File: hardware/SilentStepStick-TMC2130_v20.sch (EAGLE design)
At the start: 25 parts, among them IC1 TMC2130-LA, J1 MA08-1, J2 MA08-1, J3 MA02-1, X1 PASSER-07, X2 PASSER-07

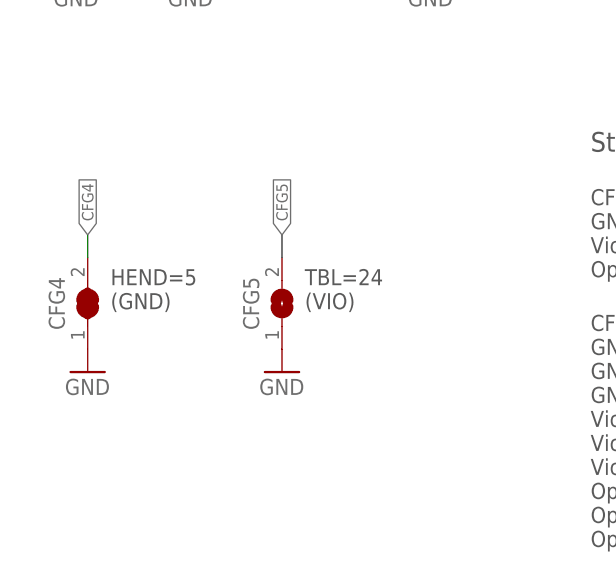
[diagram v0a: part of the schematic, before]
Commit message: updated schematics
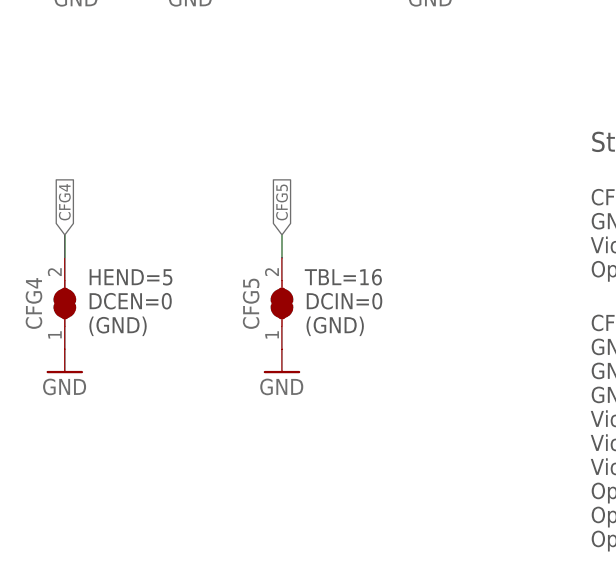
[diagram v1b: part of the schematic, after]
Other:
- note added: "HEND=5 DCEN=0 (GND)"
- note added: "TBL=16 DCIN=0 (GND)"
- note removed: "HEND=5 (GND)"
- note removed: "TBL=24 (VIO)"
- moved on the sheet: CFG4
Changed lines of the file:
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@@
 <grid distance="0.1" unitdist="inch" unit="inch" style="lines" multiple="1" display="no" altdistance="0.01" altunitdist="inch" altunit="inch"/>
 <layers>
-<layer number="1" name="Top" color="4" fill="1" visible="yes" active="no"/>
-<layer number="2" name="Route2" color="11" fill="1" visible="yes" active="no"/>
-<layer number="3" name="Route3" color="4" fill="3" visible="yes" active="no"/>
-<layer number="4" name="Route4" color="1" fill="4" visible="yes" active="no"/>
-<layer number="5" name="Route5" color="4" fill="4" visible="yes" active="no"/>
-<layer number="6" name="Route6" color="1" fill="8" visible="yes" active="no"/>
-<layer number="7" name="Route7" color="4" fill="8" visible="yes" active="no"/>
-<layer number="8" name="Route8" color="1" fill="2" visible="yes" active="no"/>
-<layer number="9" name="Route9" color="4" fill="2" visible="yes" active="no"/>
-<layer number="10" name="Route10" color="1" fill="7" visible="yes" active="no"/>
-<layer number="11" name="Route11" color="4" fill="7" visible="yes" active="no"/>
-<layer number="12" name="Route12" color="1" fill="5" visible="yes" active="no"/>
-<layer number="13" name="Route13" color="4" fill="5" visible="yes" active="no"/>
-<layer number="14" name="Route14" color="1" fill="6" visible="yes" active="no"/>
-<layer number="15" name="Route15" color="13" fill="1" visible="yes" active="no"/>
-<layer number="16" name="Bottom" color="1" fill="1" visible="yes" active="no"/>
-<layer number="17" name="Pads" color="2" fill="1" visible="yes" active="no"/>
-<layer number="18" name="Vias" color="2" fill="1" visible="yes" active="no"/>
-<layer number="19" name="Unrouted" color="14" fill="1" visible="yes" active="no"/>
-<layer number="20" name="Dimension" color="15" fill="1" visible="yes" active="no"/>
-<layer number="21" name="tPlace" color="7" fill="1" visible="yes" active="no"/>
-<layer number="22" name="bPlace" color="7" fill="1" visible="yes" active="no"/>
-<layer number="23" name="tOrigins" color="15" fill="1" visible="yes" active="no"/>
-<layer number="24" name="bOrigins" color="15" fill="1" visible="yes" active="no"/>
-<layer number="25" name="tNames" color="7" fill="1" visible="yes" active="no"/>
-<layer number="26" name="bNames" color="7" fill="1" visible="yes" active="no"/>
-<layer number="27" name="tValues" color="7" fill="1" visible="yes" active="no"/>
-<layer number="28" name="bValues" color="7" fill="1" visible="yes" active="no"/>
+<layer number="1" name="Top" color="4" fill="1" visible="no" active="no"/>
+<layer number="2" name="Route2" color="11" fill="1" visible="no" active="no"/>
+<layer number="3" name="Route3" color="4" fill="3" visible="no" active="no"/>
+<layer number="4" name="Route4" color="1" fill="4" visible="no" active="no"/>
+<layer number="5" name="Route5" color="4" fill="4" visible="no" active="no"/>
+<layer number="6" name="Route6" color="1" fill="8" visible="no" active="no"/>
+<layer number="7" name="Route7" color="4" fill="8" visible="no" active="no"/>
+<layer number="8" name="Route8" color="1" fill="2" visible="no" active="no"/>
+<layer number="9" name="Route9" color="4" fill="2" visible="no" active="no"/>
+<layer number="10" name="Route10" color="1" fill="7" visible="no" active="no"/>
+<layer number="11" name="Route11" color="4" fill="7" visible="no" active="no"/>
+<layer number="12" name="Route12" color="1" fill="5" visible="no" active="no"/>
+<layer number="13" name="Route13" color="4" fill="5" visible="no" active="no"/>
+<layer number="14" name="Route14" color="1" fill="6" visible="no" active="no"/>
+<layer number="15" name="Route15" color="13" fill="1" visible="no" active="no"/>
+<layer number="16" name="Bottom" color="1" fill="1" visible="no" active="no"/>
+<layer number="17" name="Pads" color="2" fill="1" visible="no" active="no"/>
+<layer number="18" name="Vias" color="2" fill="1" visible="no" active="no"/>
+<layer number="19" name="Unrouted" color="14" fill="1" visible="no" active="no"/>
+<layer number="20" name="Dimension" color="15" fill="1" visible="no" active="no"/>
+<layer number="21" name="tPlace" color="7" fill="1" visible="no" active="no"/>
+<layer number="22" name="bPlace" color="7" fill="1" visible="no" active="no"/>
+<layer number="23" name="tOrigins" color="15" fill="1" visible="no" active="no"/>
+<layer number="24" name="bOrigins" color="15" fill="1" visible="no" active="no"/>
+<layer number="25" name="tNames" color="7" fill="1" visible="no" active="no"/>
+<layer number="26" name="bNames" color="7" fill="1" visible="no" active="no"/>
+<layer number="27" name="tValues" color="7" fill="1" visible="no" active="no"/>
+<layer number="28" name="bValues" color="7" fill="1" visible="no" active="no"/>
 <layer number="29" name="tStop" color="7" fill="3" visible="no" active="no"/>
 <layer number="30" name="bStop" color="7" fill="6" visible="no" active="no"/>
@@
 <layer number="35" name="tGlue" color="7" fill="4" visible="no" active="no"/>
 <layer number="36" name="bGlue" color="7" fill="5" visible="no" active="no"/>
-<layer number="37" name="tTest" color="7" fill="1" visible="yes" active="no"/>
-<layer number="38" name="bTest" color="7" fill="1" visible="yes" active="no"/>
+<layer number="37" name="tTest" color="7" fill="1" visible="no" active="no"/>
+<layer number="38" name="bTest" color="7" fill="1" visible="no" active="no"/>
 <layer number="39" name="tKeepout" color="4" fill="11" visible="no" active="no"/>
 <layer number="40" name="bKeepout" color="1" fill="11" visible="no" active="no"/>
@@
 <layer number="44" name="Drills" color="7" fill="1" visible="no" active="no"/>
 <layer number="45" name="Holes" color="7" fill="1" visible="no" active="no"/>
-<layer number="46" name="Milling" color="3" fill="1" visible="yes" active="no"/>
-<layer number="47" name="Measures" color="7" fill="1" visible="yes" active="no"/>
-<layer number="48" name="Document" color="7" fill="1" visible="yes" active="no"/>
-<layer number="49" name="Reference" color="7" fill="1" visible="yes" active="no"/>
-<layer number="50" name="dxf" color="7" fill="1" visible="yes" active="no"/>
-<layer number="51" name="tDocu" color="7" fill="1" visible="yes" active="no"/>
-<layer number="52" name="bDocu" color="7" fill="1" visible="yes" active="no"/>
+<layer number="46" name="Milling" color="3" fill="1" visible="no" active="no"/>
+<layer number="47" name="Measures" color="7" fill="1" visible="no" active="no"/>
+<layer number="48" name="Document" color="7" fill="1" visible="no" active="no"/>
+<layer number="49" name="Reference" color="7" fill="1" visible="no" active="no"/>
+<layer number="50" name="dxf" color="7" fill="1" visible="no" active="no"/>
+<layer number="51" name="tDocu" color="7" fill="1" visible="no" active="no"/>
+<layer number="52" name="bDocu" color="7" fill="1" visible="no" active="no"/>
 <layer number="90" name="Modules" color="5" fill="1" visible="yes" active="yes"/>
 <layer number="91" name="Nets" color="2" fill="1" visible="yes" active="yes"/>
@@
 <layer number="98" name="Guide" color="6" fill="1" visible="yes" active="yes"/>
 <layer number="99" name="SpiceOrder" color="5" fill="1" visible="yes" active="yes"/>
-<layer number="250" name="Descript" color="3" fill="1" visible="yes" active="yes"/>
 </layers>
 <schematic xreflabel="%F%N/%S.%C%R" xrefpart="/%S.%C%R">
@@
 <sheet>
 <plain>
-<wire x1="34.29" y1="36.83" x2="34.29" y2="39.37" width="1.016" layer="94"/>
+<wire x1="31.75" y1="36.83" x2="31.75" y2="39.37" width="1.016" layer="94"/>
 <text x="162.56" y="22.86" size="1.27" layer="95" align="top-left">Released under the Creative Commons Attribution Share-Alike
 License. http://creativecommons.org/licenses/by-sa/4.0/
@@
 stealthChop</text>
 <text x="90.17" y="57.15" size="2.1844" layer="97" font="vector" ratio="10" align="top-left">Standalone Operation (SPI_MODE=GND)</text>
-<text x="36.83" y="41.91" size="1.778" layer="97" font="vector" ratio="10" align="top-left">HEND=5
+<text x="34.29" y="41.91" size="1.778" layer="97" font="vector" ratio="10" align="top-left">HEND=5
+DCEN=0
 (GND)</text>
-<text x="58.42" y="41.91" size="1.778" layer="97" font="vector" ratio="10" align="top-left">TBL=24
-(VIO)</text>
+<text x="58.42" y="41.91" size="1.778" layer="97" font="vector" ratio="10" align="top-left">TBL=16
+DCIN=0
+(GND)</text>
+<wire x1="55.88" y1="36.83" x2="55.88" y2="39.37" width="1.016" layer="94"/>
 </plain>
 <instances>
@@
 <instance part="LOGO4" gate="L" x="167.64" y="7.62"/>
 <instance part="CFG5" gate="J" x="55.88" y="38.1" rot="R90"/>
-<instance part="CFG4" gate="J" x="34.29" y="38.1" rot="R90"/>
+<instance part="CFG4" gate="J" x="31.75" y="38.1" rot="R90"/>
 <instance part="GND4" gate="1" x="55.88" y="30.48"/>
-<instance part="GND5" gate="1" x="34.29" y="30.48"/>
+<instance part="GND5" gate="1" x="31.75" y="30.48"/>
 </instances>
 <busses>
@@
 </segment>
 <segment>
-<wire x1="34.29" y1="45.72" x2="34.29" y2="43.18" width="0.1524" layer="91"/>
-<label x="34.29" y="45.72" size="1.27" layer="95" rot="R90" xref="yes"/>
+<wire x1="31.75" y1="45.72" x2="31.75" y2="43.18" width="0.1524" layer="91"/>
+<label x="31.75" y="45.72" size="1.27" layer="95" rot="R90" xref="yes"/>
 <pinref part="CFG4" gate="J" pin="2"/>
 </segment>
